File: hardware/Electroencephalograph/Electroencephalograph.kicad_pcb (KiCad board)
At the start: 2 copper layers, 100 x 100 mm, 259 parts, among them J1 Conn_01x08_Male, J2 Conn_01x08_Male, U1 ADS1298IPAG, U2 OPA330xxD, U3 TMS320LF2406PZ, U4 THI3-0511, U5 ADUM2401BRWZ, U6 TPS60403

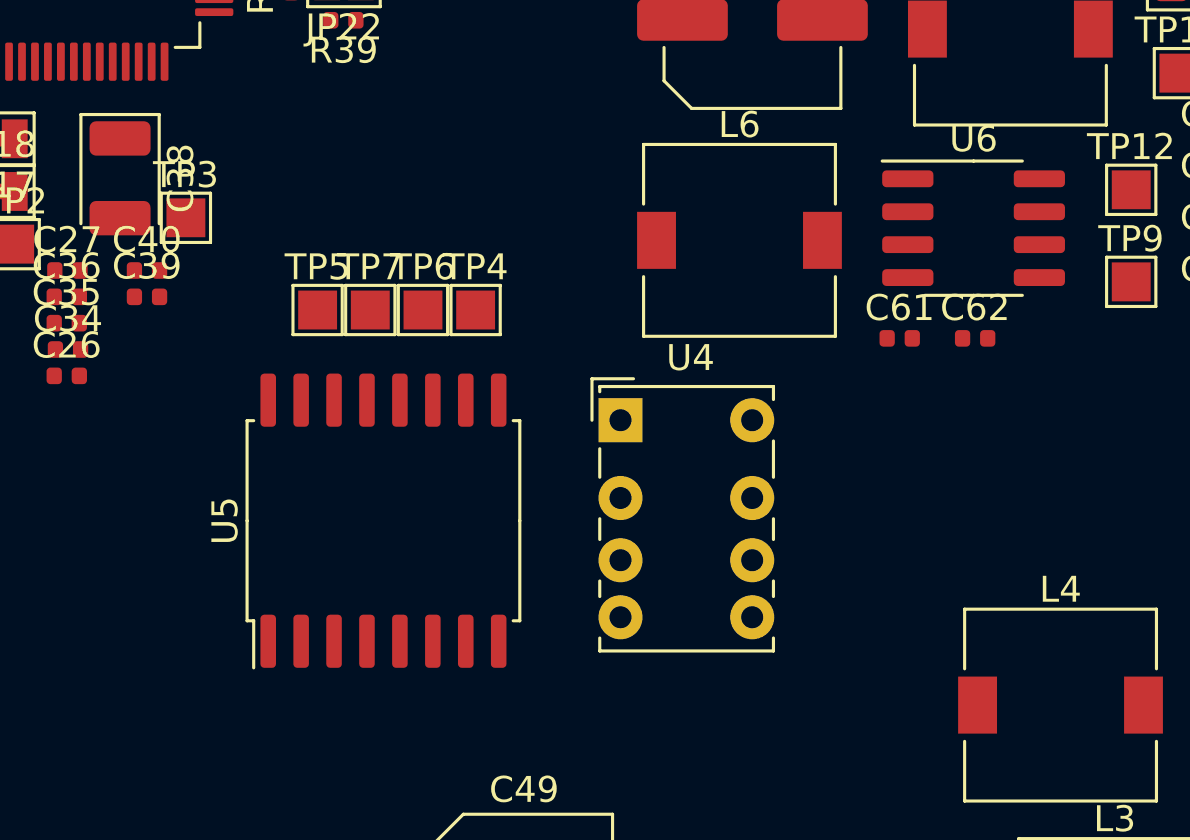
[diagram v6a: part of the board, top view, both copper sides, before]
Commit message: added dc/dc converter 3d model and footprint
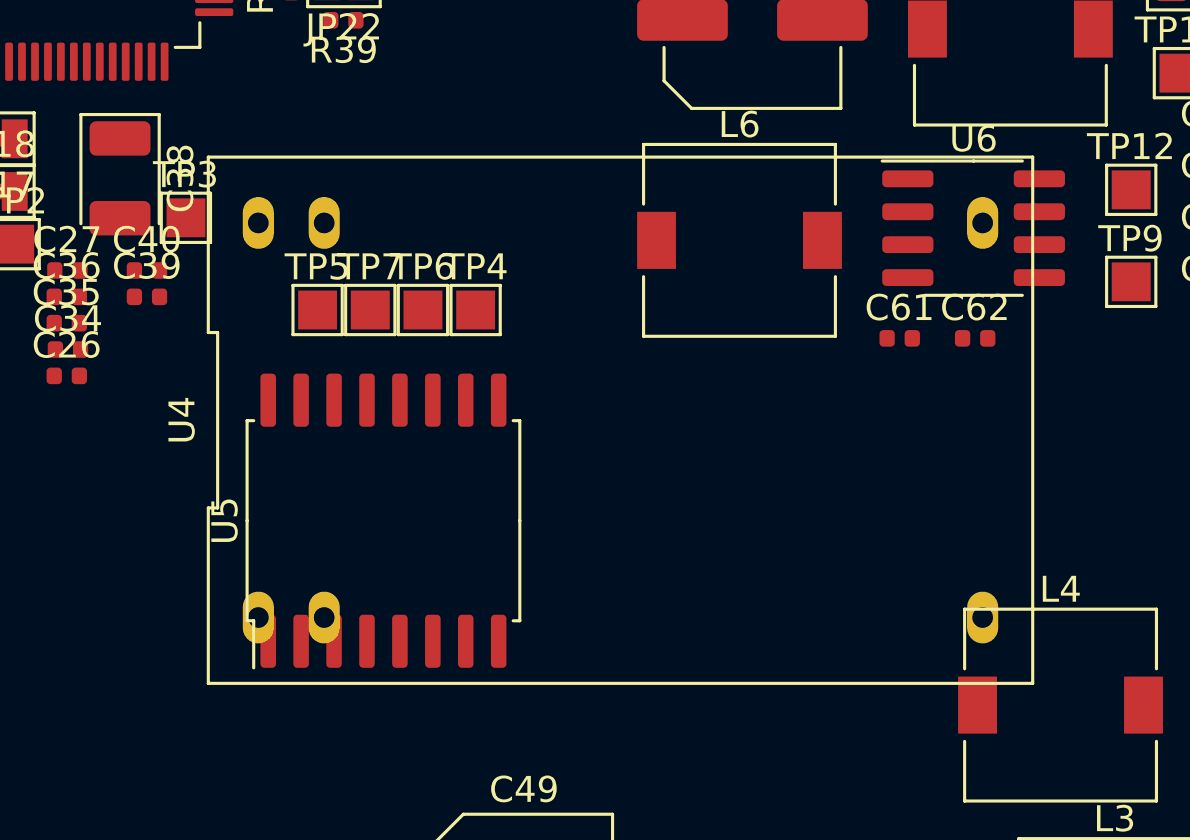
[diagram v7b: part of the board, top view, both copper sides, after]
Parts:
- U4: footprint Relay_THT:Relay_DPDT_Omron_G6K-2P-Y -> Electroencephalograph:THI3-0511
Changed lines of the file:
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@@
     (add_net VDDA)
+  )
+  (module Electroencephalograph:THI3-0511 (layer F.Cu)
+    (at 116.332 64.196)
+    (fp_text reference U4 (at -16.9 0 90) (layer F.SilkS)
+      (effects (font (size 1 1) (thickness 0.15)))
+    )
+    (fp_text value THI3-0511 (at 0 0) (layer F.Fab)
+      (effects (font (size 1 1) (thickness 0.15)))
+    )
+    (fp_line (start -14.82 8.86) (end -14.82 -8.86) (layer F.CrtYd) (width 0.05))
+    (fp_line (start 14.82 8.86) (end -14.82 8.86) (layer F.CrtYd) (width 0.05))
+    (fp_line (start 14.82 -8.86) (end 14.82 8.86) (layer F.CrtYd) (width 0.05))
+    (fp_line (start -14.82 -8.86) (end 14.82 -8.86) (layer F.CrtYd) (width 0.05))
+    (fp_line (start -15.9 3.383333) (end -15.9 10.149999) (layer F.SilkS) (width 0.12))
+    (fp_line (start -15.54 3.383333) (end -15.9 3.383333) (layer F.SilkS) (width 0.12))
+    (fp_line (start -15.54 -3.383333) (end -15.54 3.383333) (layer F.SilkS) (width 0.12))
+    (fp_line (start -15.9 -3.383333) (end -15.54 -3.383333) (layer F.SilkS) (width 0.12))
+    (fp_line (start -15.9 -10.15) (end -15.9 -3.383333) (layer F.SilkS) (width 0.12))
+    (fp_line (start 15.9 -10.149999) (end -15.9 -10.15) (layer F.SilkS) (width 0.12))
+    (fp_line (start 15.9 10.15) (end 15.9 -10.149999) (layer F.SilkS) (width 0.12))
+    (fp_line (start -15.9 10.149999) (end 15.9 10.15) (layer F.SilkS) (width 0.12))
+    (pad 12 thru_hole oval (at 13.97 7.61) (size 1.2 2) (drill 0.8) (layers *.Cu *.Mask)
+      (net 1 GNDA))
+    (pad 13 thru_hole oval (at 13.97 -7.61) (size 1.2 2) (drill 0.8) (layers *.Cu *.Mask)
+      (net 79 "Net-(C52-Pad1)"))
+    (pad 2 thru_hole oval (at -11.43 7.61) (size 1.2 2) (drill 0.8) (layers *.Cu *.Mask)
+      (net 78 "Net-(C50-Pad1)"))
+    (pad 23 thru_hole oval (at -11.43 -7.61) (size 1.2 2) (drill 0.8) (layers *.Cu *.Mask)
+      (net 1 GNDA))
+    (pad 1 thru_hole oval (at -13.97 7.61) (size 1.2 2) (drill 0.8) (layers *.Cu *.Mask)
+      (net 78 "Net-(C50-Pad1)"))
+    (pad 24 thru_hole oval (at -13.97 -7.61) (size 1.2 2) (drill 0.8) (layers *.Cu *.Mask)
+      (net 1 GNDA))
+    (model "${KIPRJMOD}/3DModels/THI 3-0511.step"
+      (at (xyz 0 0 0))
+      (scale (xyz 1 1 1))
+      (rotate (xyz 0 0 0))
+    )
   )
   (module Package_SO:SOP-8_3.76x4.96mm_P1.27mm (layer F.Cu)
@@
       (at (xyz 0 0 0))
       (scale (xyz 1 1 1))
-      (rotate (xyz 0 0 0))
-    )
-  )
-  (module Relay_THT:Relay_DPDT_Omron_G6K-2P-Y (layer F.Cu)
-    (at 116.332 64.196)
-    (descr "Omron G6K-2P-Y relay package http://omronfs.omron.com/en_US/ecb/products/pdf/en-g6k.pdf")
-    (tags "Omron G6K-2P-Y relay")
-    (fp_text reference U4 (at 2.7 -2.4) (layer F.SilkS)
-      (effects (font (size 1 1) (thickness 0.15)))
-    )
-    (fp_text value THI3-0511 (at 2.5 10.1) (layer F.Fab)
-      (effects (font (size 1 1) (thickness 0.15)))
-    )
-    (fp_line (start 6.18 9.05) (end -1.1 9.05) (layer F.CrtYd) (width 0.05))
-    (fp_line (start 6.18 9.05) (end 6.18 -1.45) (layer F.CrtYd) (width 0.05))
-    (fp_line (start -1.1 -1.45) (end -1.1 9.05) (layer F.CrtYd) (width 0.05))
-    (fp_line (start -1.1 -1.45) (end 6.18 -1.45) (layer F.CrtYd) (width 0.05))
-    (fp_line (start 0.3 -1.2) (end 5.8 -1.2) (layer F.Fab) (width 0.12))
-    (fp_line (start 5.8 -1.2) (end 5.8 8.8) (layer F.Fab) (width 0.12))
-    (fp_line (start 5.8 8.8) (end -0.7 8.8) (layer F.Fab) (width 0.12))
-    (fp_line (start -0.7 8.8) (end -0.7 -0.2) (layer F.Fab) (width 0.12))
-    (fp_line (start -0.7 -0.2) (end 0.3 -1.2) (layer F.Fab) (width 0.12))
-    (fp_line (start -0.8 -1.3) (end 5.9 -1.3) (layer F.SilkS) (width 0.12))
-    (fp_line (start 5.9 -1.3) (end 5.9 -0.8) (layer F.SilkS) (width 0.12))
-    (fp_line (start 5.9 0.8) (end 5.9 2.2) (layer F.SilkS) (width 0.12))
-    (fp_line (start 5.9 3.8) (end 5.9 4.6) (layer F.SilkS) (width 0.12))
-    (fp_line (start 5.9 6.2) (end 5.9 6.8) (layer F.SilkS) (width 0.12))
-    (fp_line (start 5.9 8.4) (end 5.9 8.9) (layer F.SilkS) (width 0.12))
-    (fp_line (start 5.9 8.9) (end -0.8 8.9) (layer F.SilkS) (width 0.12))
-    (fp_line (start -0.8 8.9) (end -0.8 8.4) (layer F.SilkS) (width 0.12))
-    (fp_line (start -0.8 6.8) (end -0.8 6.2) (layer F.SilkS) (width 0.12))
-    (fp_line (start -0.8 4.6) (end -0.8 3.8) (layer F.SilkS) (width 0.12))
-    (fp_line (start -0.8 2.2) (end -0.8 1.1) (layer F.SilkS) (width 0.12))
-    (fp_line (start -0.8 -1.3) (end -0.8 -1.1) (layer F.SilkS) (width 0.12))
-    (fp_line (start -1.1 0) (end -1.1 -1.6) (layer F.SilkS) (width 0.12))
-    (fp_line (start -1.1 -1.6) (end 0.5 -1.6) (layer F.SilkS) (width 0.12))
-    (fp_text user %R (at 2.55 3.8) (layer F.Fab)
-      (effects (font (size 1 1) (thickness 0.15)))
-    )
-    (pad 1 thru_hole rect (at 0 0) (size 1.7 1.7) (drill 0.85) (layers *.Cu *.Mask)
-      (net 78 "Net-(C50-Pad1)"))
-    (pad 2 thru_hole circle (at 0 3) (size 1.7 1.7) (drill 0.85) (layers *.Cu *.Mask)
-      (net 78 "Net-(C50-Pad1)"))
-    (pad 3 thru_hole circle (at 0 5.4) (size 1.7 1.7) (drill 0.85) (layers *.Cu *.Mask))
-    (pad 4 thru_hole circle (at 0 7.6) (size 1.7 1.7) (drill 0.85) (layers *.Cu *.Mask))
-    (pad 5 thru_hole circle (at 5.08 7.6) (size 1.7 1.7) (drill 0.85) (layers *.Cu *.Mask))
-    (pad 6 thru_hole circle (at 5.08 5.4) (size 1.7 1.7) (drill 0.85) (layers *.Cu *.Mask))
-    (pad 7 thru_hole circle (at 5.08 3) (size 1.7 1.7) (drill 0.85) (layers *.Cu *.Mask))
-    (pad 8 thru_hole circle (at 5.08 0) (size 1.7 1.7) (drill 0.85) (layers *.Cu *.Mask))
-    (model ${KISYS3DMOD}/Relay_THT.3dshapes/Relay_DPDT_Omron_G6K-2P-Y.wrl
-      (at (xyz 0 0 0))
-      (scale (xyz 1 1 1))

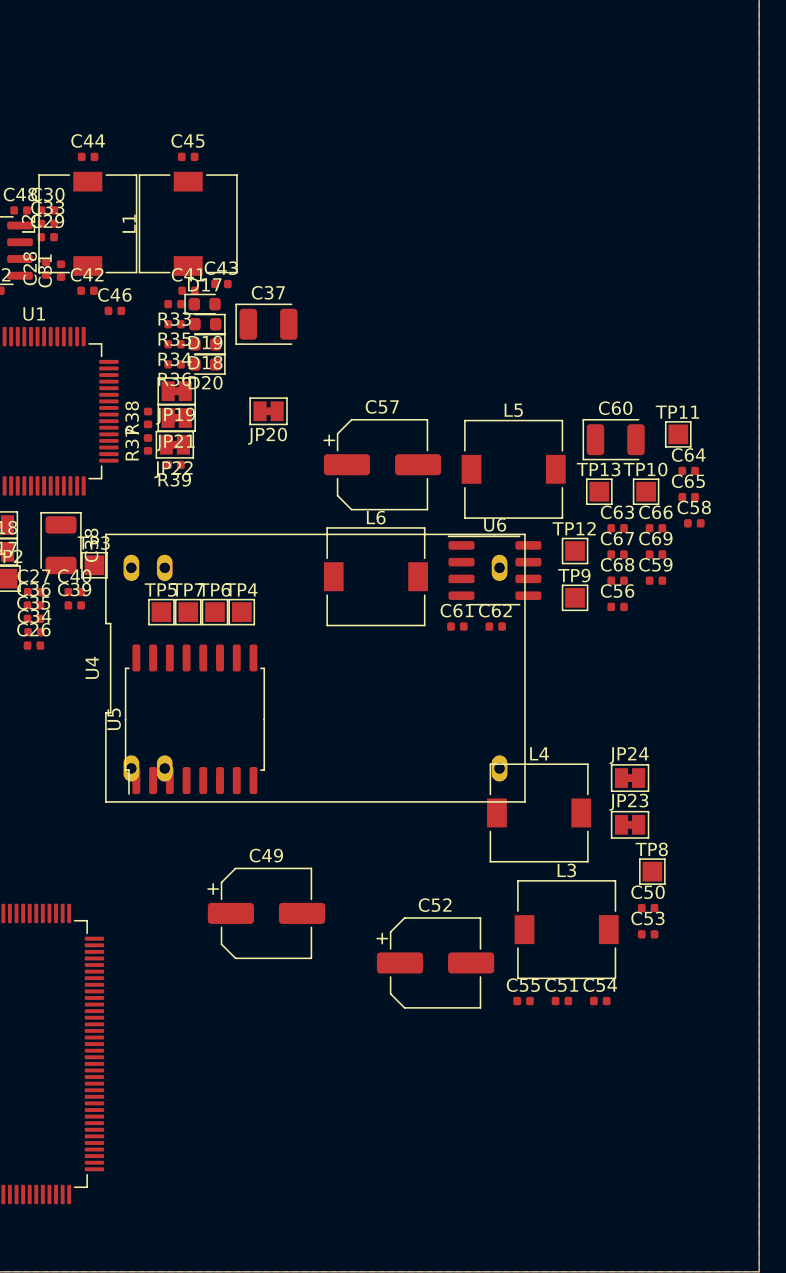
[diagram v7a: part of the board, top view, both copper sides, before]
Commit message: added inductor 3d model
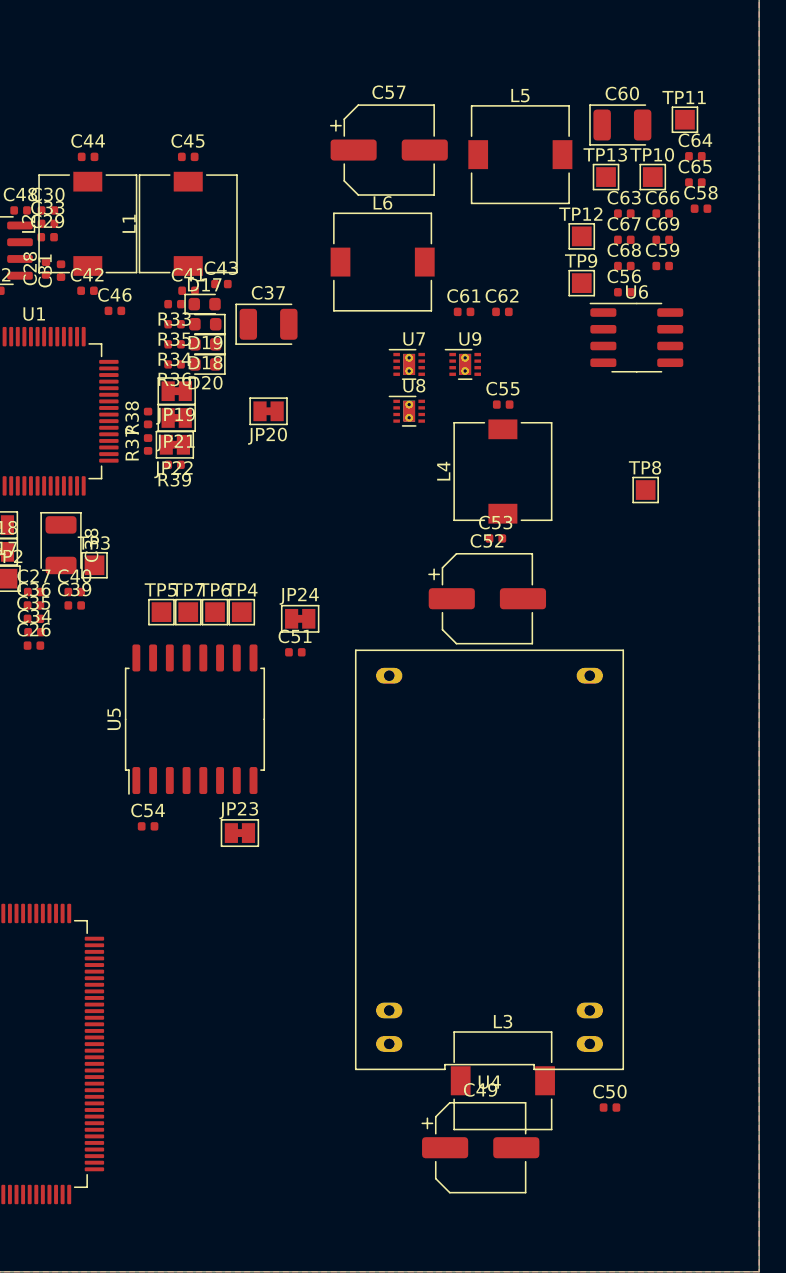
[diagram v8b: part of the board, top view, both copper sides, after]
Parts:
- added U7: LP5912-1.8DRVT, Package_SON:WSON-8-1EP_2x2mm_P0.5mm_EP0.9x1.6mm_ThermalVias, F.Cu at (123.4, 41.1)
- added U8: LP5912-1.8DRVT, Package_SON:WSON-8-1EP_2x2mm_P0.5mm_EP0.9x1.6mm_ThermalVias, F.Cu at (123.4, 44.7)
- added U9: LP5912-1.8DRVT, Package_SON:WSON-8-1EP_2x2mm_P0.5mm_EP0.9x1.6mm_ThermalVias, F.Cu at (127.7, 41.1)
- L1, L2, L3, L4, L5, L6: footprint Inductor_SMD:L_7.3x7.3_H3.5 -> Electroencephalograph:L_7.3x7.3_H3.5
- moved C55 45.3 mm to (130.6, 44.2)
- moved C54 36.8 mm to (103.6, 76.2)
- moved C51 33.3 mm to (114.8, 63.0)
- moved C53 32.2 mm to (130.0, 54.4)
- moved JP23 29.6 mm to (110.6, 76.7)
- moved TP8 29.0 mm to (141.4, 50.7)
- moved C52 27.9 mm to (129.4, 58.9)
- moved JP24 27.8 mm to (115.2, 60.5)
- moved L4 26.1 mm to (130.6, 49.3), turned to 90 degrees
- moved C49 24.1 mm to (128.9, 100.6)
- moved C56 23.9 mm to (139.8, 35.7)
- moved C65 23.9 mm to (145.2, 27.3)
- moved L6 23.9 mm to (121.4, 33.4)
- moved C57 23.9 mm to (121.9, 24.9)
- moved C63 23.9 mm to (139.8, 29.7)
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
